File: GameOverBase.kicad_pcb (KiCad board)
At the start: 4 copper layers, 50 x 30 mm, 49 parts, among them J1 USB_C_DEALON-USB-US31-106, J2 Serial Port, J3 add-on conn, Q1 PMN48XP, SW1 SW_DIP_x08, SW2 boot, SW3 Reset, U1 ESP32-WROOM-E, U2 4021, U3 MCP73831-2ACI-OT, U4 XC6210B332MR

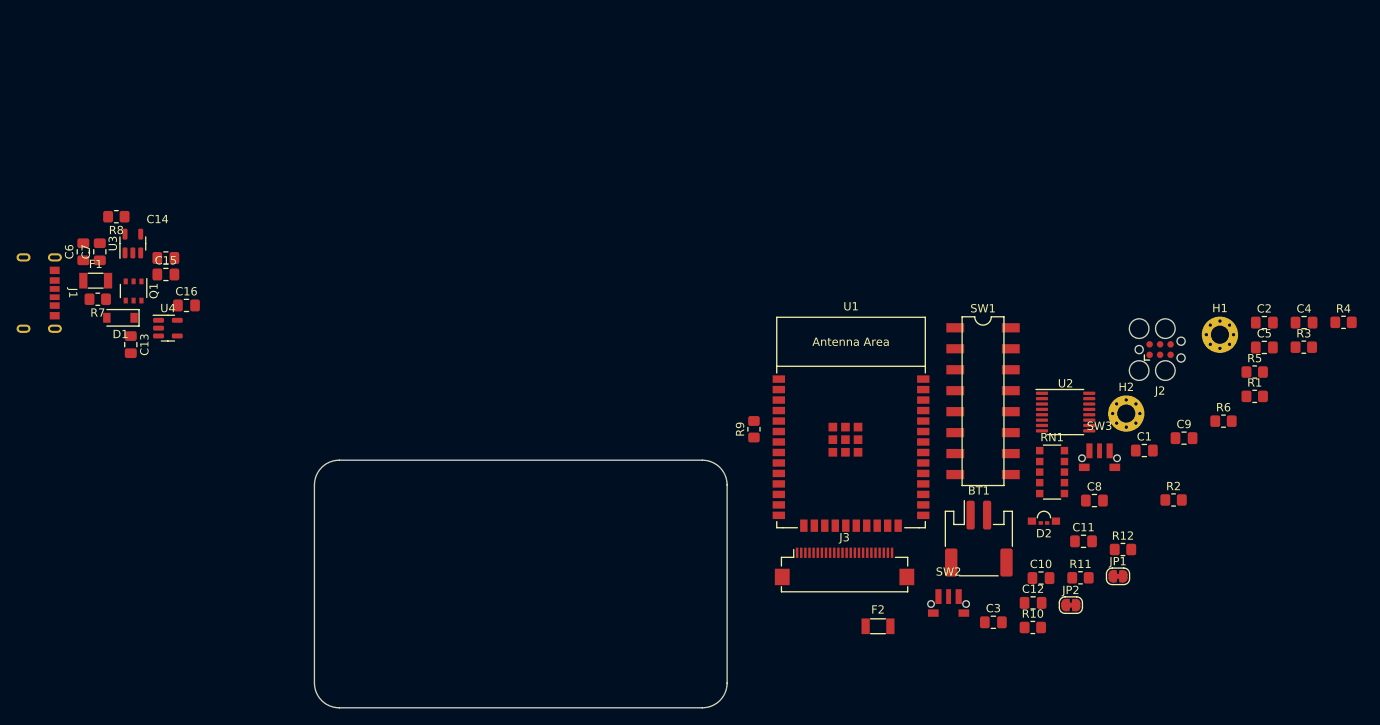
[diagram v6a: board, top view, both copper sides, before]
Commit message: Includes missing components in the power block
I missed the battery connector, the fuse and the battery sensing voltage
divider.
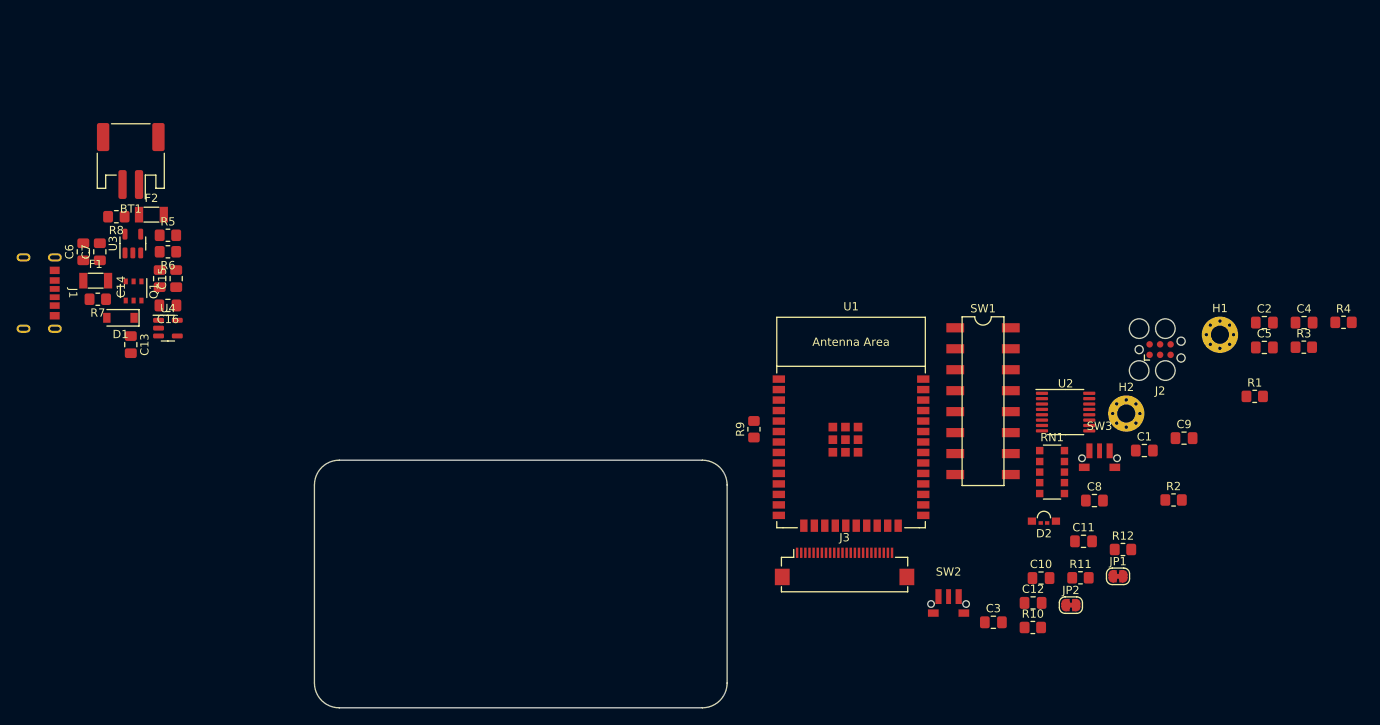
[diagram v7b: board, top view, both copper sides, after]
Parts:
- moved R5 132.7 mm to (102.2, 52.8)
- moved R6 129.5 mm to (102.2, 54.8), turned to 180 degrees
- moved BT1 112.5 mm to (97.8, 43.8), turned to 180 degrees
- moved F2 101.2 mm to (100.2, 50.2)
- moved C14 2.61 mm to (101.2, 58.0), turned to 90 degrees
- moved C16 2.25 mm to (102.2, 61.2), turned to 180 degrees
- moved C15 1.35 mm to (103.2, 58.0), turned to 90 degrees
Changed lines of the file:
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@@
   )
   (footprint "Capacitor_SMD:C_0805_2012Metric_Pad1.18x1.45mm_HandSolder" (layer "F.Cu")
-    (at 102 55.5)
+    (at 101.25 58 90)
     (descr "Capacitor SMD 0805 (2012 Metric), square (rectangular) end terminal, IPC_7351 nominal with elongated pad for handsoldering. (Body size source: IPC-SM-782 page 76, https://www.pcb-3d.com/wordpress/wp-content/uploads/ipc-sm-782a_amendment_1_and_2.pdf, https://docs.google.com/spreadsheets/d/1BsfQQcO9C6DZCsRaXUlFlo91Tg2WpOkGARC1WS5S8t0/edit?usp=sharing), generated with kicad-footprint-generator")
     (tags "capacitor handsolder")
@@
     (property "Sheetname" "")
     (attr smd)
-    (fp_text reference "C14" (at -1 -4.68) (layer "F.SilkS")
-        (effects (font (size 1 1) (thickness 0.15)))
-    )
-    (fp_text value "10µF" (at 0 1.68) (layer "F.Fab")
-        (effects (font (size 1 1) (thickness 0.15)))
-    )
-    (fp_text user "${REFERENCE}" (at -1 -3) (layer "F.Fab")
+    (fp_text reference "C14" (at -1 -4.68 90) (layer "F.SilkS")
+        (effects (font (size 1 1) (thickness 0.15)))
+    )
+    (fp_text value "10µF" (at 0 1.68 90) (layer "F.Fab")
+        (effects (font (size 1 1) (thickness 0.15)))
+    )
+    (fp_text user "${REFERENCE}" (at -1 -3 90) (layer "F.Fab")
         (effects (font (size 0.5 0.5) (thickness 0.08)))
     )
@@
     (fp_line (start 1 0.625) (end -1 0.625)
       (stroke (width 0.1) (type solid)) (layer "F.Fab"))
-    (pad "1" smd roundrect (at -1.0375 0) (size 1.175 1.45) (layers "F.Cu" "F.Paste" "F.Mask") (roundrect_rratio 0.212766)
+    (pad "1" smd roundrect (at -1.0375 0 90) (size 1.175 1.45) (layers "F.Cu" "F.Paste" "F.Mask") (roundrect_rratio 0.212766)
       (net 9 "+BATT") (pintype "passive"))
-    (pad "2" smd roundrect (at 1.0375 0) (size 1.175 1.45) (layers "F.Cu" "F.Paste" "F.Mask") (roundrect_rratio 0.212766)
+    (pad "2" smd roundrect (at 1.0375 0 90) (size 1.175 1.45) (layers "F.Cu" "F.Paste" "F.Mask") (roundrect_rratio 0.212766)
       (net 2 "GND") (pintype "passive"))
     (model "${KICAD6_3DMODEL_DIR}/Capacitor_SMD.3dshapes/C_0805_2012Metric.wrl"
@@
   )
   (footprint "Capacitor_SMD:C_0805_2012Metric_Pad1.18x1.45mm_HandSolder" (layer "F.Cu")
-    (at 104.5 61.25)
+    (at 102.25 61.25 180)
     (descr "Capacitor SMD 0805 (2012 Metric), square (rectangular) end terminal, IPC_7351 nominal with elongated pad for handsoldering. (Body size source: IPC-SM-782 page 76, https://www.pcb-3d.com/wordpress/wp-content/uploads/ipc-sm-782a_amendment_1_and_2.pdf, https://docs.google.com/spreadsheets/d/1BsfQQcO9C6DZCsRaXUlFlo91Tg2WpOkGARC1WS5S8t0/edit?usp=sharing), generated with kicad-footprint-generator")
     (tags "capacitor handsolder")
@@
     (fp_line (start 1 0.625) (end -1 0.625)
       (stroke (width 0.1) (type solid)) (layer "F.Fab"))
-    (pad "1" smd roundrect (at -1.0375 0) (size 1.175 1.45) (layers "F.Cu" "F.Paste" "F.Mask") (roundrect_rratio 0.212766)
+    (pad "1" smd roundrect (at -1.0375 0 180) (size 1.175 1.45) (layers "F.Cu" "F.Paste" "F.Mask") (roundrect_rratio 0.212766)
       (net 3 "+3V3") (pintype "passive"))
-    (pad "2" smd roundrect (at 1.0375 0) (size 1.175 1.45) (layers "F.Cu" "F.Paste" "F.Mask") (roundrect_rratio 0.212766)
+    (pad "2" smd roundrect (at 1.0375 0 180) (size 1.175 1.45) (layers "F.Cu" "F.Paste" "F.Mask") (roundrect_rratio 0.212766)
       (net 2 "GND") (pintype "passive"))
     (model "${KICAD6_3DMODEL_DIR}/Capacitor_SMD.3dshapes/C_0805_2012Metric.wrl"
@@
   )
   (footprint "GameOver:Belfuse_0ZCJ" (layer "F.Cu")
-    (at 188.28 100.12)
+    (at 100.25 50.25)
     (property "Sheetfile" "GameOverBase.kicad_sch")
     (property "Sheetname" "")
@@
   )
   (footprint "Resistor_SMD:R_0805_2012Metric_Pad1.20x1.40mm_HandSolder" (layer "F.Cu")
-    (at 230.14 75.27)
+    (at 102.25 54.75 180)
     (descr "Resistor SMD 0805 (2012 Metric), square (rectangular) end terminal, IPC_7351 nominal with elongated pad for handsoldering. (Body size source: IPC-SM-782 page 72, https://www.pcb-3d.com/wordpress/wp-content/uploads/ipc-sm-782a_amendment_1_and_2.pdf), generated with kicad-footprint-generator")
     (tags "resistor handsolder")
@@
     (fp_line (start 1 0.625) (end -1 0.625)
       (stroke (width 0.1) (type solid)) (layer "F.Fab"))
-    (pad "1" smd roundrect (at -1 0) (size 1.2 1.4) (layers "F.Cu" "F.Paste" "F.Mask") (roundrect_rratio 0.208333)
+    (pad "1" smd roundrect (at -1 0 180) (size 1.2 1.4) (layers "F.Cu" "F.Paste" "F.Mask") (roundrect_rratio 0.208333)
       (net 6 "BAT_SENSE") (pintype "passive"))
-    (pad "2" smd roundrect (at 1 0) (size 1.2 1.4) (layers "F.Cu" "F.Paste" "F.Mask") (roundrect_rratio 0.208333)
+    (pad "2" smd roundrect (at 1 0 180) (size 1.2 1.4) (layers "F.Cu" "F.Paste" "F.Mask") (roundrect_rratio 0.208333)
       (net 2 "GND") (pintype "passive"))
     (model "${KICAD6_3DMODEL_DIR}/Resistor_SMD.3dshapes/R_0805_2012Metric.wrl"
@@
   )
   (footprint "Connector_JST:JST_PH_S2B-PH-SM4-TB_1x02-1MP_P2.00mm_Horizontal" (layer "F.Cu")
-    (at 200.5 89.5)
+    (at 97.75 43.75 180)
     (descr "JST PH series connector, S2B-PH-SM4-TB (http://www.jst-mfg.com/product/pdf/eng/ePH.pdf), generated with kicad-footprint-generator")
     (tags "connector JST PH top entry")
@@
     (fp_line (start 3.95 -3.2) (end 3.95 4.4)
       (stroke (width 0.1) (type solid)) (layer "F.Fab"))
-    (pad "1" smd roundrect (at -1 -2.85) (size 1 3.5) (layers "F.Cu" "F.Paste" "F.Mask") (roundrect_rratio 0.25)
+    (pad "1" smd roundrect (at -1 -2.85 180) (size 1 3.5) (layers "F.Cu" "F.Paste" "F.Mask") (roundrect_rratio 0.25)
       (net 1 "Net-(BT1-+)") (pinfunction "+") (pintype "passive"))
-    (pad "2" smd roundrect (at 1 -2.85) (size 1 3.5) (layers "F.Cu" "F.Paste" "F.Mask") (roundrect_rratio 0.25)
+    (pad "2" smd roundrect (at 1 -2.85 180) (size 1 3.5) (layers "F.Cu" "F.Paste" "F.Mask") (roundrect_rratio 0.25)
       (net 2 "GND") (pinfunction "-") (pintype "passive"))
-    (pad "MP" smd roundrect (at -3.35 2.9) (size 1.5 3.4) (layers "F.Cu" "F.Paste" "F.Mask") (roundrect_rratio 0.166667))
-    (pad "MP" smd roundrect (at 3.35 2.9) (size 1.5 3.4) (layers "F.Cu" "F.Paste" "F.Mask") (roundrect_rratio 0.166667))
+    (pad "MP" smd roundrect (at -3.35 2.9 180) (size 1.5 3.4) (layers "F.Cu" "F.Paste" "F.Mask") (roundrect_rratio 0.166667))
+    (pad "MP" smd roundrect (at 3.35 2.9 180) (size 1.5 3.4) (layers "F.Cu" "F.Paste" "F.Mask") (roundrect_rratio 0.166667))
     (model "${KICAD6_3DMODEL_DIR}/Connector_JST.3dshapes/JST_PH_S2B-PH-SM4-TB_1x02-1MP_P2.00mm_Horizontal.wrl"
       (offset (xyz 0 0 0))
@@
   )
   (footprint "Resistor_SMD:R_0805_2012Metric_Pad1.20x1.40mm_HandSolder" (layer "F.Cu")
-    (at 233.92 69.32)
+    (at 102.25 52.75)
     (descr "Resistor SMD 0805 (2012 Metric), square (rectangular) end terminal, IPC_7351 nominal with elongated pad for handsoldering. (Body size source: IPC-SM-782 page 72, https://www.pcb-3d.com/wordpress/wp-content/uploads/ipc-sm-782a_amendment_1_and_2.pdf), generated with kicad-footprint-generator")
     (tags "resistor handsolder")
@@
   )
   (footprint "Capacitor_SMD:C_0805_2012Metric_Pad1.18x1.45mm_HandSolder" (layer "F.Cu")
-    (at 102 57.5)
+    (at 103.25 58 90)
     (descr "Capacitor SMD 0805 (2012 Metric), square (rectangular) end terminal, IPC_7351 nominal with elongated pad for handsoldering. (Body size source: IPC-SM-782 page 76, https://www.pcb-3d.com/wordpress/wp-content/uploads/ipc-sm-782a_amendment_1_and_2.pdf, https://docs.google.com/spreadsheets/d/1BsfQQcO9C6DZCsRaXUlFlo91Tg2WpOkGARC1WS5S8t0/edit?usp=sharing), generated with kicad-footprint-generator")
     (tags "capacitor handsolder")
@@
     (property "Sheetname" "")
     (attr smd)
-    (fp_text reference "C15" (at 0 -1.68) (layer "F.SilkS")
-        (effects (font (size 1 1) (thickness 0.15)))
-    )
-    (fp_text value "100nF" (at 0 1.68) (layer "F.Fab")
-        (effects (font (size 1 1) (thickness 0.15)))
-    )
-    (fp_text user "${REFERENCE}" (at 0 0) (layer "F.Fab")
+    (fp_text reference "C15" (at 0 -1.68 90) (layer "F.SilkS")
+        (effects (font (size 1 1) (thickness 0.15)))
+    )
+    (fp_text value "100nF" (at 0 1.68 90) (layer "F.Fab")
+        (effects (font (size 1 1) (thickness 0.15)))
+    )
+    (fp_text user "${REFERENCE}" (at 0 0 90) (layer "F.Fab")
         (effects (font (size 0.5 0.5) (thickness 0.08)))
     )
@@
     (fp_line (start 1 0.625) (end -1 0.625)
       (stroke (width 0.1) (type solid)) (layer "F.Fab"))
-    (pad "1" smd roundrect (at -1.0375 0) (size 1.175 1.45) (layers "F.Cu" "F.Paste" "F.Mask") (roundrect_rratio 0.212766)
+    (pad "1" smd roundrect (at -1.0375 0 90) (size 1.175 1.45) (layers "F.Cu" "F.Paste" "F.Mask") (roundrect_rratio 0.212766)
       (net 9 "+BATT") (pintype "passive"))
-    (pad "2" smd roundrect (at 1.0375 0) (size 1.175 1.45) (layers "F.Cu" "F.Paste" "F.Mask") (roundrect_rratio 0.212766)
+    (pad "2" smd roundrect (at 1.0375 0 90) (size 1.175 1.45) (layers "F.Cu" "F.Paste" "F.Mask") (roundrect_rratio 0.212766)
       (net 2 "GND") (pintype "passive"))
     (model "${KICAD6_3DMODEL_DIR}/Capacitor_SMD.3dshapes/C_0805_2012Metric.wrl"

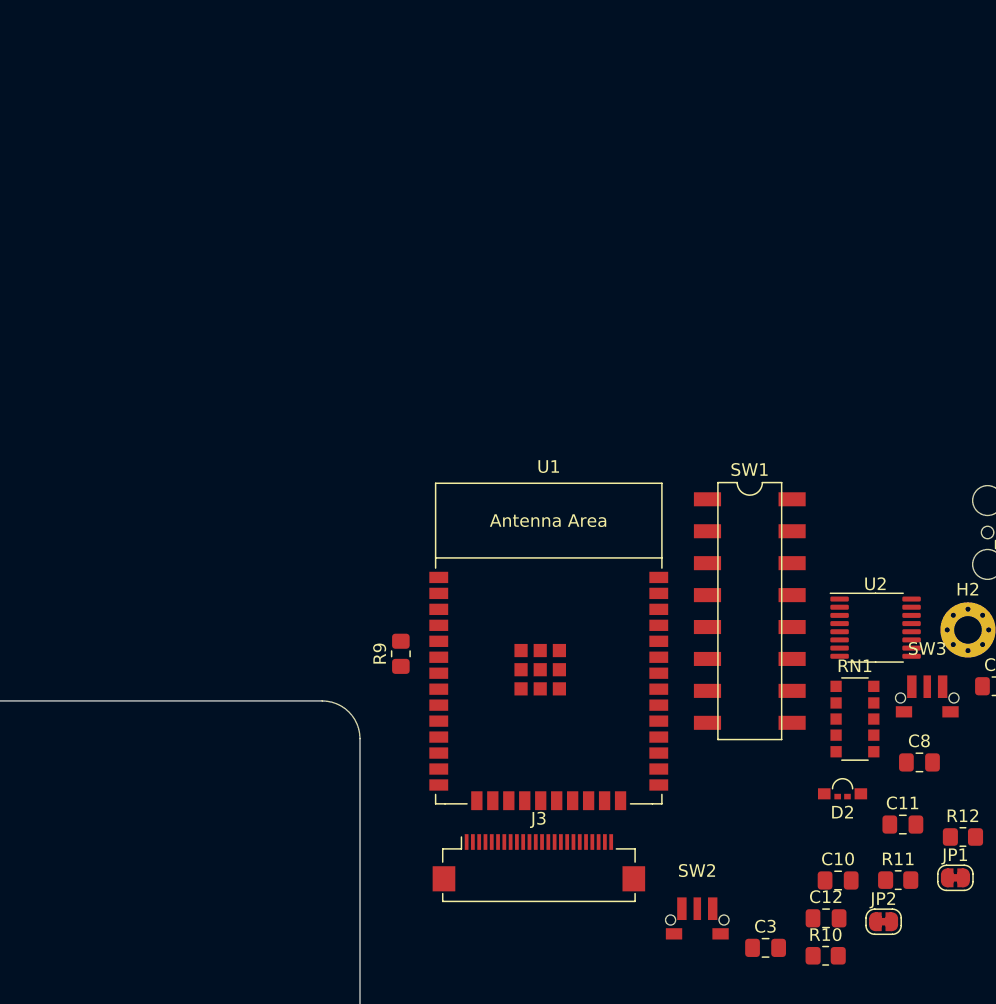
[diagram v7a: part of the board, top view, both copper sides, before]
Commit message: Groups together board ID circuit
The positioning of components is still very rough as with the power
circuit. The routing needs to be redone, it's there just to check if the
component positions make any sense.
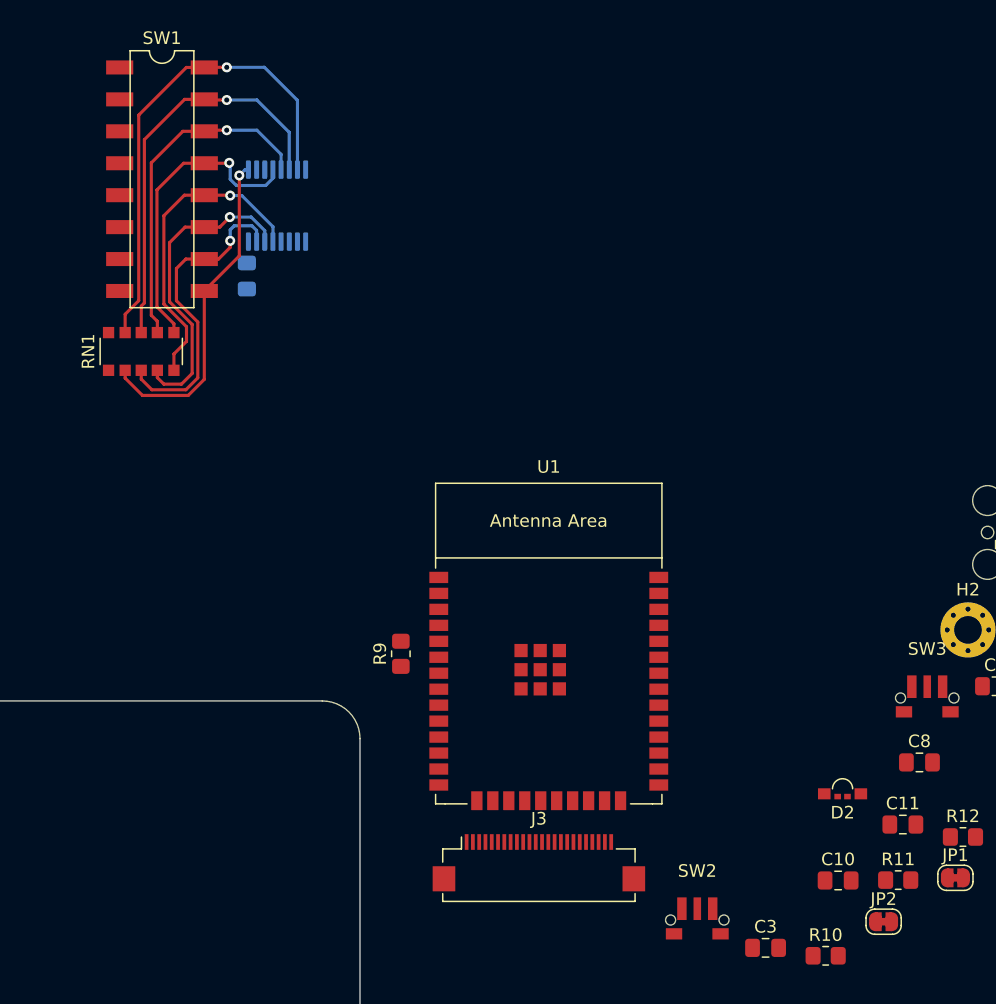
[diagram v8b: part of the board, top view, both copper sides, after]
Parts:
- C12, U2: moved to B.Cu
- moved C12 68.8 mm to (161.0, 46.2), turned to -90 degrees
- moved RN1 63.9 mm to (152.6, 52.2), turned to 90 degrees
- moved U2 58.3 mm to (163.4, 40.6), turned to -90 degrees
- moved SW1 58.0 mm to (154.2, 38.5)
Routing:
- net Net-(RN1-R8): track 0.00 -> 38.5 mm, vias 0 -> 1
- net Net-(RN1-R7): track 0.00 -> 32.4 mm, vias 0 -> 1
- net Net-(RN1-R6): track 0.00 -> 27.1 mm, vias 0 -> 1
- net Net-(RN1-R1): track 0.00 -> 26.3 mm, vias 0 -> 1
- net Net-(RN1-R4): track 0.00 -> 25.0 mm, vias 0 -> 1
- net Net-(RN1-R2): track 0.00 -> 25.0 mm, vias 0 -> 1
- net Net-(RN1-R3): track 0.00 -> 24.8 mm, vias 0 -> 1
- net Net-(RN1-R5): track 0.00 -> 24.4 mm, vias 0 -> 1
